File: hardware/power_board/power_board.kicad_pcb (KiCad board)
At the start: 2 copper layers, 110 x 80 mm, 0 parts

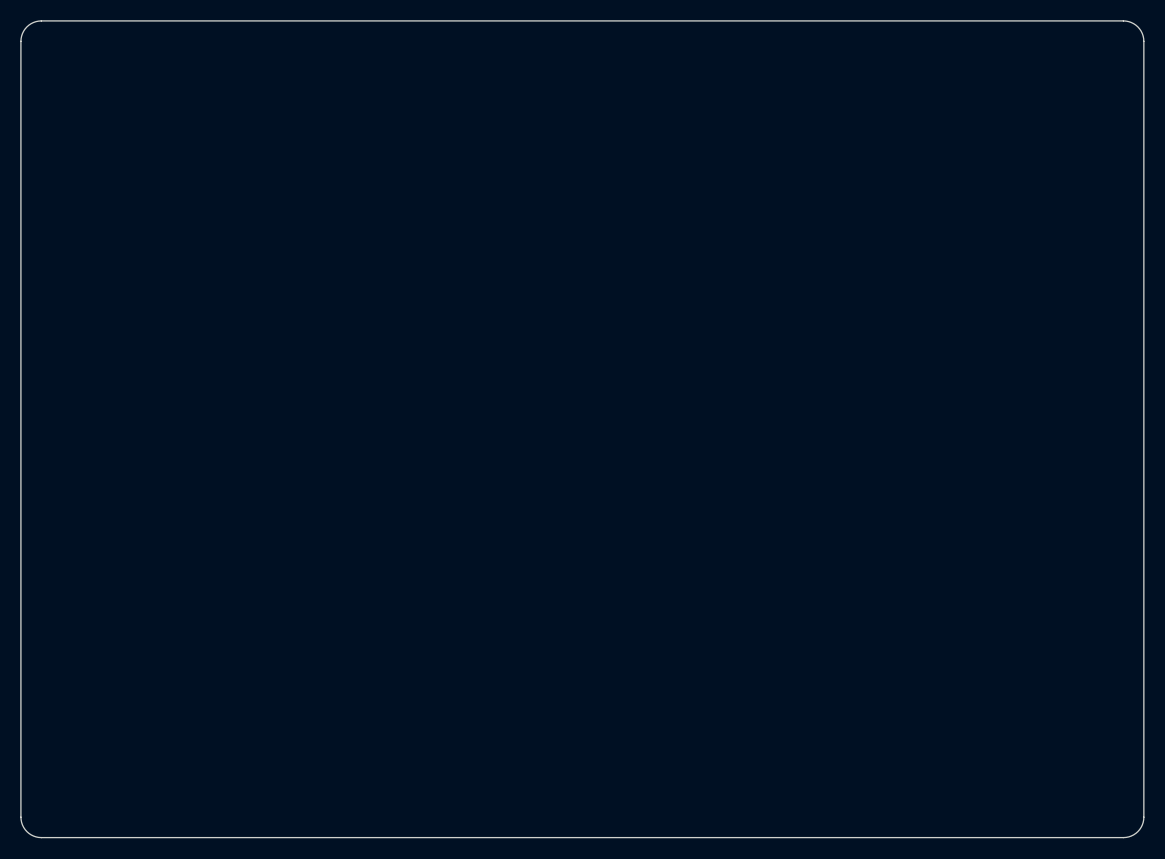
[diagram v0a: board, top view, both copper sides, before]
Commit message: PCBs routed, labelled and ready to order: Rev 1 fabrication files and buy list
Both boards placed, routed and finished by script (hardware/gen): layout.sh places
(placement.py, with silkscreen names for every terminal, port, header and button),
route.sh routes with Freerouting inside rule areas and net classes from the layout
guide and keeps a board only with 0 DRC errors, 0 unconnected and exact schematic
parity, routespec.sh checks what the DRC cannot (planes, crystal, converter loop,
IPC-2221 widths), finish.sh adds the bottom-silkscreen identification and writes
the fabrication files (gerbers, drill, BOM, positions) only when the DRC passes.

- Pod 70 x 53 mm, 4 layers: In1 solid GND, In2 +3V3, 530 teardrops; no DRC warnings.
- Power 95 x 66 mm, 2 layers, 2 oz: 10 A rail as a zone, converter re-placed (switch
  node 16 mm, feedback 7 mm, no vias; was 78 mm and 40 mm), 328 teardrops.
- Screw terminals turned to open outward; RESET/BOOT side-push on the pod's left
  edge; USB-C footprint with a 3D model (GCT USB4105).
- Pod J2 now the Adafruit 4754's JP1 row pin for pin (the old order shorted its
  3.3 V output to ground); IMU reset on a new J8; HC-05 header fed 5 V.
- Buy list per footprint and module connections in bill-of-materials.md section 10.
- LAYOUT_GUIDE rewritten as how the boards were routed and how to review them;
  decisions, progress log and BUILD_GUIDE updated; power box follows the wider board.
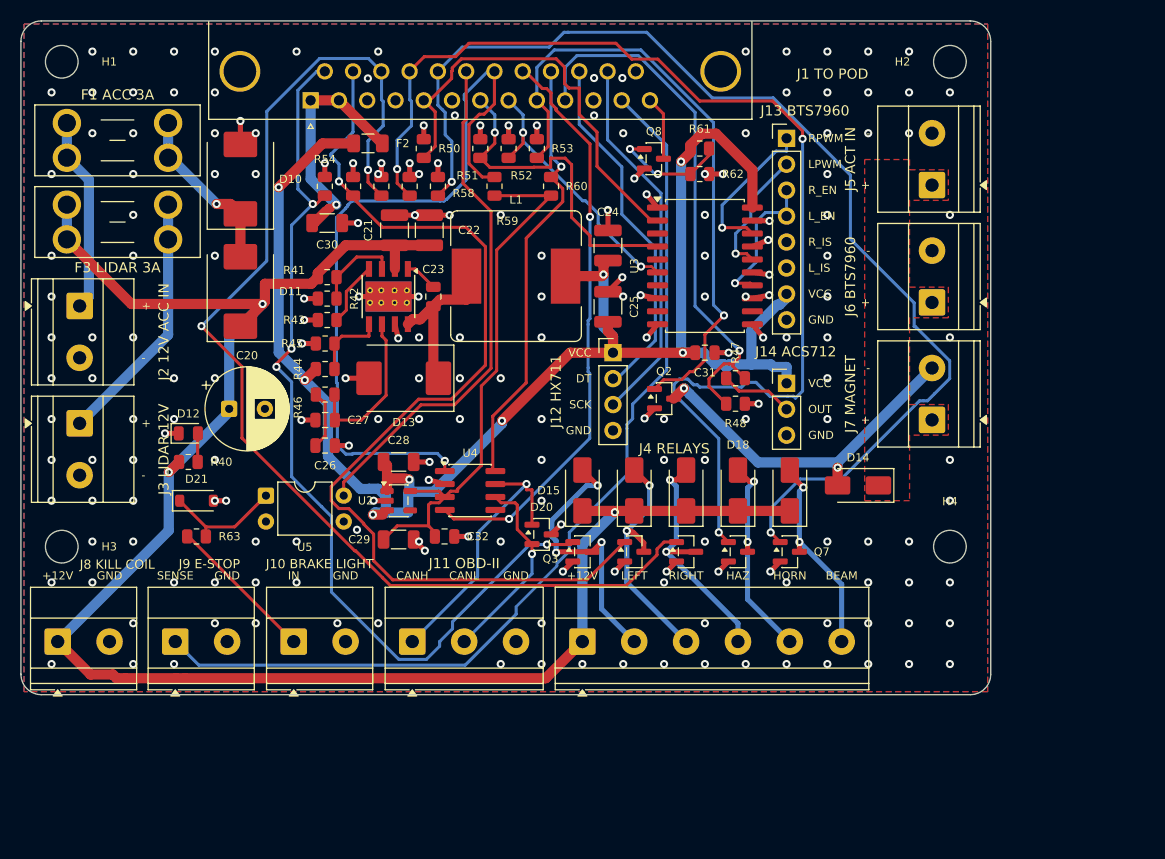
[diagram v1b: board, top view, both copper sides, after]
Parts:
- added C20: 47u 63V, Capacitor_THT:CP_Radial_D8.0mm_P3.50mm, F.Cu at (70.4, 88.0)
- added C21: 2.2u 100V, Capacitor_SMD:C_1210_3225Metric, F.Cu at (86.6, 70.5)
- added C22: 2.2u 100V, Capacitor_SMD:C_1210_3225Metric, F.Cu at (90.0, 70.5)
- added C23: 100n, Capacitor_SMD:C_0805_2012Metric, F.Cu at (90.4, 77.0)
- added C24: 47u, Capacitor_SMD:C_1210_3225Metric, F.Cu at (107.5, 72.0)
- added C25: 47u, Capacitor_SMD:C_1210_3225Metric, F.Cu at (107.5, 78.0)
- added C26: 6800p, Capacitor_SMD:C_0805_2012Metric, F.Cu at (79.8, 91.6)
- added C27: 39p, Capacitor_SMD:C_0805_2012Metric, F.Cu at (79.8, 89.1)
- added C28: 10u, Capacitor_SMD:C_1206_3216Metric, F.Cu at (87.0, 93.2)
- added C29: 10u, Capacitor_SMD:C_1206_3216Metric, F.Cu at (87.0, 100.8)
- added C30: 10u, Capacitor_SMD:C_1206_3216Metric, F.Cu at (80.0, 69.8)
- added C31: 100n, Capacitor_SMD:C_0805_2012Metric, F.Cu at (117.0, 82.5)
- added C32: 100n, Capacitor_SMD:C_0805_2012Metric, F.Cu at (91.5, 100.5)
- added D10: SMCJ24CA, Diode_SMD:D_SMC, F.Cu at (71.5, 65.5)
- added D11: B560C, Diode_SMD:D_SMC, F.Cu at (71.5, 76.5)
- added D12: green, LED_SMD:LED_0805_2012Metric, F.Cu at (66.4, 90.4)
- added D13: B560C, Diode_SMD:D_SMC, F.Cu at (87.5, 85.0)
- added D14: SS14, Diode_SMD:D_SMA, F.Cu at (132.0, 95.5)
- added D15: SS14, Diode_SMD:D_SMA, F.Cu at (105.0, 96.0)
- added D16: SS14, Diode_SMD:D_SMA, F.Cu at (110.1, 96.0)
- added D17: SS14, Diode_SMD:D_SMA, F.Cu at (115.2, 96.0)
- added D18: SS14, Diode_SMD:D_SMA, F.Cu at (120.2, 96.0)
- added D19: SS14, Diode_SMD:D_SMA, F.Cu at (125.3, 96.0)
- added D20: NUP2105L, Package_TO_SOT_SMD:SOT-23, F.Cu at (101.0, 100.3)
- added D21: 1N4148W, Diode_SMD:D_SOD-123, F.Cu at (67.2, 97.0)
- added F1: 3A, Fuse:Fuseholder_Blade_Mini_Keystone_3568, F.Cu at (54.5, 60.0)
- added F2: 500mA, Fuse:Fuse_1206_3216Metric, F.Cu at (84.0, 62.0)
- added F3: 3A, Fuse:Fuseholder_Blade_Mini_Keystone_3568, F.Cu at (54.5, 68.0)
- added H1: M3, MountingHole:MountingHole_3.2mm_M3, F.Cu at (54.0, 54.0)
- added H2: M3, MountingHole:MountingHole_3.2mm_M3, F.Cu at (141.0, 54.0)
- added H3: M3, MountingHole:MountingHole_3.2mm_M3, F.Cu at (54.0, 101.5)
- added H4: M3, MountingHole:MountingHole_3.2mm_M3, F.Cu at (141.0, 101.5)
- added J1: DB-25 to pod, Connector_Dsub:DSUB-25_Socket_Horizontal_P2.77x2.84mm_EdgePinOffset4.94mm_Housed_MountingHolesOffset4.94mm, F.Cu at (78.4, 57.8)
- added J10: Brake-light switch, TerminalBlock_Phoenix:TerminalBlock_Phoenix_MKDS-1,5-2-5.08_1x02_P5.08mm_Horizontal, F.Cu at (76.7, 110.8)
- added J11: OBD-II lead, TerminalBlock_Phoenix:TerminalBlock_Phoenix_MKDS-1,5-3-5.08_1x03_P5.08mm_Horizontal, F.Cu at (88.3, 110.8)
- added J12: Bench: HX711, Connector_PinHeader_2.54mm:PinHeader_1x04_P2.54mm_Vertical, F.Cu at (108.0, 82.5)
- added J13: BTS7960 module, Connector_PinHeader_2.54mm:PinHeader_1x08_P2.54mm_Vertical, F.Cu at (125.0, 61.5)
- added J14: ACS712 module, Connector_PinHeader_2.54mm:PinHeader_1x03_P2.54mm_Vertical, F.Cu at (125.0, 85.5)
- added J2: 12 V ACC in, TerminalBlock_Phoenix:TerminalBlock_Phoenix_MKDS-1,5-2-5.08_1x02_P5.08mm_Horizontal, F.Cu at (55.8, 77.9)
- added J3: LiDAR 12 V out, TerminalBlock_Phoenix:TerminalBlock_Phoenix_MKDS-1,5-2-5.08_1x02_P5.08mm_Horizontal, F.Cu at (55.8, 89.4)
- added J4: Relay coils, TerminalBlock_Phoenix:TerminalBlock_Phoenix_MKDS-1,5-6-5.08_1x06_P5.08mm_Horizontal, F.Cu at (105.0, 110.8)
- added J5: Actuator 12 V from kill relay, TerminalBlock_Phoenix:TerminalBlock_Phoenix_MKDS-1,5-2-5.08_1x02_P5.08mm_Horizontal, F.Cu at (139.2, 66.1)
- added J6: BTS7960 B+ / B-, TerminalBlock_Phoenix:TerminalBlock_Phoenix_MKDS-1,5-2-5.08_1x02_P5.08mm_Horizontal, F.Cu at (139.2, 77.6)
- added J7: Cable magnet, TerminalBlock_Phoenix:TerminalBlock_Phoenix_MKDS-1,5-2-5.08_1x02_P5.08mm_Horizontal, F.Cu at (139.2, 89.1)
- added J8: Kill relay coil feed, TerminalBlock_Phoenix:TerminalBlock_Phoenix_MKDS-1,5-2-5.08_1x02_P5.08mm_Horizontal, F.Cu at (53.6, 110.8)
- added J9: E-stop sense contact, TerminalBlock_Phoenix:TerminalBlock_Phoenix_MKDS-1,5-2-5.08_1x02_P5.08mm_Horizontal, F.Cu at (65.1, 110.8)
- added L1: 8.2u, Inductor_SMD:L_Bourns_SRR1260, F.Cu at (98.5, 75.0)
- added Q2: AO3400A, Package_TO_SOT_SMD:SOT-23, F.Cu at (113.0, 87.0)
- added Q3: AO3400A, Package_TO_SOT_SMD:SOT-23, F.Cu at (105.0, 102.0)
- added Q4: AO3400A, Package_TO_SOT_SMD:SOT-23, F.Cu at (110.1, 102.0)
- added Q5: AO3400A, Package_TO_SOT_SMD:SOT-23, F.Cu at (115.2, 102.0)
- added Q6: AO3400A, Package_TO_SOT_SMD:SOT-23, F.Cu at (120.2, 102.0)
- added Q7: AO3400A, Package_TO_SOT_SMD:SOT-23, F.Cu at (125.3, 102.0)
- added Q8: 2N7002, Package_TO_SOT_SMD:SOT-23, F.Cu at (112.0, 63.5)
- added R40: 4.7k, Resistor_SMD:R_0805_2012Metric, F.Cu at (66.4, 93.2)
- added R41: 523k, Resistor_SMD:R_0805_2012Metric, F.Cu at (80.0, 75.1)
- added R42: 84.5k, Resistor_SMD:R_0805_2012Metric, F.Cu at (80.0, 77.2)
- added R43: 162k, Resistor_SMD:R_0805_2012Metric, F.Cu at (80.0, 79.3)
- added R44: 53.6k, Resistor_SMD:R_0805_2012Metric, F.Cu at (79.8, 84.1)
- added R45: 10.2k, Resistor_SMD:R_0805_2012Metric, F.Cu at (79.8, 81.6)
- added R46: 13.0k, Resistor_SMD:R_0805_2012Metric, F.Cu at (79.8, 86.6)
- added R47: 10k, Resistor_SMD:R_0805_2012Metric, F.Cu at (120.0, 85.0)
- added R48: 20k, Resistor_SMD:R_0805_2012Metric, F.Cu at (120.0, 87.5)
- added R50: 10k, Resistor_SMD:R_0805_2012Metric, F.Cu at (89.5, 62.5)
- added R51: 10k, Resistor_SMD:R_0805_2012Metric, F.Cu at (95.0, 62.5)
- added R52: 10k, Resistor_SMD:R_0805_2012Metric, F.Cu at (97.8, 62.5)
- added R53: 10k, Resistor_SMD:R_0805_2012Metric, F.Cu at (100.5, 62.5)
- added R54: 10k, Resistor_SMD:R_0805_2012Metric, F.Cu at (79.8, 66.2)
- added R55: 10k, Resistor_SMD:R_0805_2012Metric, F.Cu at (82.5, 66.2)
- added R56: 10k, Resistor_SMD:R_0805_2012Metric, F.Cu at (85.3, 66.2)
- added R57: 10k, Resistor_SMD:R_0805_2012Metric, F.Cu at (88.1, 66.2)
- added R58: 10k, Resistor_SMD:R_0805_2012Metric, F.Cu at (90.8, 66.2)
- added R59: 10k, Resistor_SMD:R_0805_2012Metric, F.Cu at (96.4, 66.2)
- added R60: 10k, Resistor_SMD:R_0805_2012Metric, F.Cu at (101.9, 66.2)
- added R61: 10k, Resistor_SMD:R_0805_2012Metric, F.Cu at (116.5, 62.5)
- added R62: 100k, Resistor_SMD:R_0805_2012Metric, F.Cu at (116.5, 65.0)
- added R63: 2.2k, Resistor_SMD:R_0805_2012Metric, F.Cu at (67.2, 100.5)
- added U1: TPS54360DDA, Package_SO:TI_SO-PowerPAD-8_ThermalVias, F.Cu at (86.0, 77.0)
- added U2: AP2112K-3.3, Package_TO_SOT_SMD:SOT-23-5, F.Cu at (87.0, 97.0)
- added U3: 74HCT244, Package_SO:SOIC-20W_7.5x12.8mm_P1.27mm, F.Cu at (117.0, 74.0)
- added U4: SN65HVD230, Package_SO:SOIC-8_3.9x4.9mm_P1.27mm, F.Cu at (94.0, 96.0)
- added U5: PC817, Package_DIP:DIP-4_W7.62mm, F.Cu at (74.0, 96.5)
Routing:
- net +12V: track 0.00 -> 182.2 mm, vias 0 -> 3
- net +5V: track 0.00 -> 165.4 mm, vias 0 -> 8
- net /RELAY_HAZARD: track 0.00 -> 114.2 mm, vias 0 -> 2
- net /RELAY_HORN: track 0.00 -> 113.9 mm, vias 0 -> 3
- net /RELAY_BEAM: track 0.00 -> 111.6 mm, vias 0 -> 2
- net /RELAY_RIGHT: track 0.00 -> 97.2 mm, vias 0 -> 1
- net /KILL_SENSE: track 0.00 -> 94.7 mm
- net /RELAY_LEFT: track 0.00 -> 90.2 mm, vias 0 -> 4
- net GND: track 0.00 -> 79.0 mm, vias 0 -> 200
- net /CAN_TX: track 0.00 -> 74.6 mm, vias 0 -> 1
- net /MAGNET_EN: track 0.00 -> 61.3 mm, vias 0 -> 1
- net /CAN_RX: track 0.00 -> 57.1 mm, vias 0 -> 2
- net +3V3: track 0.00 -> 53.6 mm
- net /BRAKE_CURRENT: track 0.00 -> 53.4 mm, vias 0 -> 1
- net /BRAKE_LIGHT: track 0.00 -> 50.7 mm
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- added copper zone on F.Cu, net /Brake actuator: buffer, BTS7960, current sense, cable magnet/ACT_12V
- added copper zone on B.Cu, net GND
- added copper zone on F.Cu, net GND
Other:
- board size 110 x 80 mm -> 95 x 66 mm
- board text added: "+"
- board text added: "+12V"
- board text added: "-"
- board text added: "AR WINDSCREEN - POWER BOARD"
- board text added: "Actuator terminals J5-J7 + module headers J13, J14: right edge"
- board text added: "BEAM"
- board text added: "CANH"
- board text added: "CANL"
- board text added: "Car-wiring terminals J8-J11, J4: bottom edge"
- board text added: "DT"
- board text added: "F1 ACC 3A"
- board text added: "F3 LIDAR 3A"
- board text added: "Fuse holders F1, F3: top-left"
- board text added: "GND"
- board text added: "HAZ"
- board text added: "HORN"
- board text added: "I. K. MWENDA (FINAL YEAR PROJECT)"
- board text added: "IN"
- board text added: "Input and LiDAR terminals J2, J3: left edge"
- board text added: "J1 TO POD"
- board text added: "J10 BRAKE LIGHT"
- board text added: "J11 OBD-II"
- board text added: "J12 HX711"
- board text added: "J13 BTS7960"
- board text added: "J14 ACS712"
- board text added: "J2 12V ACC IN"
- board text added: "J3 LIDAR 12V"
- board text added: "J4 RELAYS"
- board text added: "J5 ACT IN"
- board text added: "J6 BTS7960"
- board text added: "J7 MAGNET"
- board text added: "J8 KILL COIL"
- board text added: "J9 E-STOP"
- board text added: "LEFT"
- board text added: "LPWM"
- board text added: "L_EN"
- board text added: "L_IS"
- board text added: "OUT"
- board text added: "REV 1 2026-10"
- board text added: "RIGHT"
- board text added: "RPWM"
- board text added: "R_EN"
- board text added: "R_IS"
- board text added: "SCK"
- board text added: "SENSE"
- board text added: "VCC"
- board text added: "power_board: 95 x 66 mm, 2 layers. 2 layers, order 2 oz (70 um) copper. TPS54360 loop compact (datasheet layout). Outline and holes from hardware/gen/outlines.py (shared with the enclosures)."
- board text removed: "BTS7960 / ACS712 module headers J13, J14: right edge"
- board text removed: "Fuse holders F1, F3: top edge, left"
- board text removed: "Terminal blocks J2-J11: bottom edge (all car-side wiring)"
- board text removed: "power_board: 110 x 80 mm, 2 layers. 2 layers, order 2 oz (70 um) copper. TPS54360 loop compact (datasheet layout). Outline and holes from hardware/gen/outlines.py (shared with the enclosures)."

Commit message: Review fixes: no via in SMD pads, 0.6 mm round terminal pins; 5 V converter simulated
An engineer's review of the Rev 1 boards: a via on a ground pad, and thin tracks
close to the screw terminals. Both measured true (9 vias touching ground pads on
the power board, 2 on the pod; 5 places within 0.3 mm of a terminal pin).

- route.py: no via touches any surface-mount pad (stitching and mending had let a
  via sit on its own net's pad); 0.6 mm round terminal and fuse-holder pins, given
  to Freerouting as grown pad copies (KiCad does not export a pad's own clearance);
  layout.py sets that clearance on the real pads for the DRC.
- routespec.sh checks both rules; both boards rerouted, teardrops re-added,
  finished: DRC 0 errors, 0 unconnected, parity exact; all checks pass.
- hardware/sim: the power board's TPS54360 converter simulated with TI's own
  transient model and the board's values, in KiCad's ngspice (no install):
  start-up, a 0.2-1.5 A load step (stability) and 9-30 V input, all within the
  stated limits. TI's model is downloaded on use, not committed.
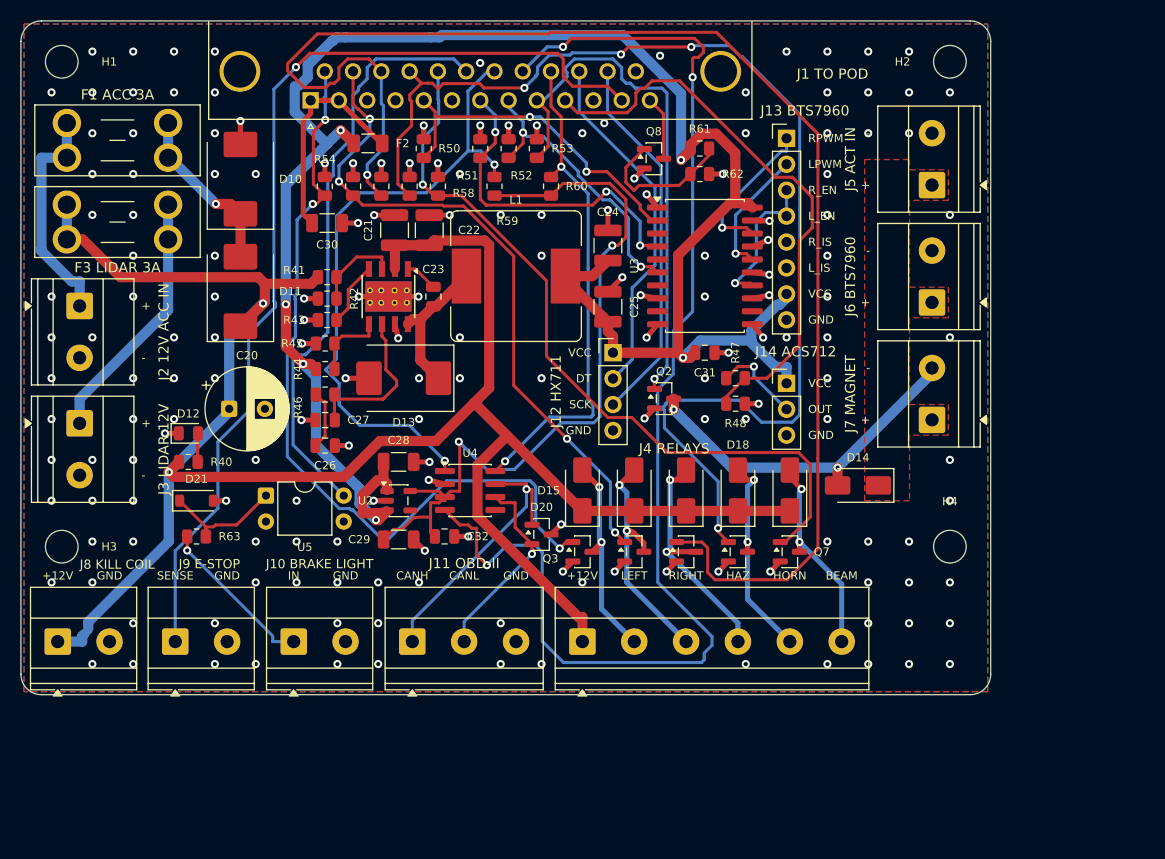
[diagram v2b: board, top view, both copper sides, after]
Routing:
- net /CAN_RX: track 57.1 -> 124.0 mm, vias 2 -> 3
- net /RELAY_BEAM: track 111.6 -> 74.5 mm, vias 2 -> 1
- net /RELAY_RIGHT: track 97.2 -> 65.5 mm, vias 1 -> 4
- net /RELAY_HAZARD: track 114.2 -> 142.4 mm, vias 2 -> 1
- net +5V: track 165.4 -> 189.1 mm, vias 8 -> 6
- net +3V3: track 53.6 -> 74.8 mm, vias 0 -> 2
- net +12V: track 182.2 -> 201.8 mm, vias 3 -> 2
- net /CAN_TX: track 74.6 -> 62.3 mm, vias 1 -> 2
- net /RELAY_LEFT: track 90.2 -> 79.7 mm, vias 4 -> 3
- net /BRAKE_RPWM: track 42.7 -> 33.3 mm, vias 0 -> 2
- net /MAGNET_EN: track 61.3 -> 53.3 mm
- net /BRAKE_LIGHT: track 50.7 -> 58.2 mm
- net /Signal relays: indicators, hazards, horn, high beam/COIL_LEFT: track 27.3 -> 20.2 mm, vias 3 -> 2
- net /CAN_STBY: track 43.4 -> 48.6 mm, vias 1 -> 2
- net /12 V input and protection/ACC_IN: track 19.2 -> 22.4 mm
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
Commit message: TVS D10 now SMCJ33CA; 12 V input protection simulated
hardware/sim/run_input.sh simulates the power board's input (3 A fuse, TVS,
B560C reverse diode, C20) against ISO 16750-2 and ISO 7637-2 for a 12 V car:
normal running, reversed battery, 24 V jump-start, the centrally suppressed load
dump (35 V for 400 ms) and pulses 1 and 2a. The SMCJ24CA first chosen breaks
down at ~27 V, so in the suppressed load dump it tried to hold the car's whole
supply down (~100 ms at up to 141 W, near its rating). The SMCJ33CA breaks down
at ~37 V: it stays idle through that dump (rail at most 33 V; the buck, C20 and
D11 are rated 60 V or more) and still clamps the fast spikes. Same SMC
footprint: only the value changed, copper and teardrops untouched.

Also: the pod's J8 had no off-board wiring entry for the assembly documents.
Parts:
- D10: value SMCJ24CA -> SMCJ33CA

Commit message: Enclosures, brake-light and pod-supply simulations, R63/C1/C2 values, report drafts
Enclosures (hardware/enclosures/): the E-stop housing (yellow ASA box for the 22 mm
mushroom, M16 gland, base to a dash panel), the windscreen pod (rear cover, front shell
whose carrier wall holds board and camera, black front plate with hood, cradle with a
+-8 deg pitch lock on a rail, glass plate template) and the gesture puck (APDS-9960
module under an open window, VHB base). Typical part dimensions are marked VERIFY.
Every STL is a manifold solid.

Simulations: run_brake.sh (PC817 input through the cable to PB5: thresholds with the
weakest and strongest optocoupler, reversed wiring, jump-start, load dump, timing) and
run_pod_supply.sh (cable +5 V and USB diode-OR into the AP2112K: worst cable, lowest
USB, cable pulled while running, USB inrush, back-feed). Both ALL PASS.

Adopted from them, value changes only (copper and teardrops untouched, fab files
regenerated, DRC 0/0, parity exact): power board R63 2.2k -> 4.7k (237 mW in a 24 V
jump-start, beyond the 0805's 125 mW; now 111 mW) and pod C1/C2 10u -> 1u/4.7u (USB
attach inrush 88 uC against USB 2.0's 50 uC; now 28 uC). Order from this commit: the
pcb-rev1.1 tag predates these two changes.

Report: docs/report/final/ drafts Part 16.1 sections 2-6 and 11 from the design as
built, with [RESULT]/[FIGURE]/[CHECK] slots where tests or decisions are pending.
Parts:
- R63: value 2.2k -> 4.7k
